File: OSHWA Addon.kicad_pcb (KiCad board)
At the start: 2 copper layers, 33.3 x 40.6 mm, 5 parts, among them J1 Conn_02x02_Counter_Clockwise

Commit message: update silkscreen text
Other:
- board text added: "Andrew Sowa (@junesphd)"
- board text added: "github.com/OSHPark/ ohs18addon"
- board text removed: "Andrew Sowa OSHWA Summit 2018 MIT"
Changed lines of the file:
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@@
-(kicad_pcb (version 20171130) (host pcbnew "(5.0.0)")
+(kicad_pcb (version 20171130) (host pcbnew 5.0.0-fee4fd1~65~ubuntu17.10.1)
   (general
     (thickness 1.6)
-    (drawings 45)
+    (drawings 46)
     (tracks 3)
     (zones 0)
@@
   (page A4)
   (layers
-    (0 F.Cu signal)
-    (31 B.Cu signal)
+    (0 F.Cu signal hide)
+    (31 B.Cu signal hide)
     (32 B.Adhes user)
     (33 F.Adhes user)
@@
       (xy -2.549664 -1.91989) (xy -2.469928 -1.911165) (xy -2.400256 -1.919918)) (layer B.SilkS) (width 0.01))
   )
+  (gr_text "github.com/OSHPark/\nohs18addon" (at 25.49 29.22 90) (layer B.SilkS)
+    (effects (font (size 1 1) (thickness 0.25)) (justify mirror))
+  )
   (gr_text D (at 26 12.73 90) (layer B.SilkS)
     (effects (font (size 1.5 1.5) (thickness 0.3)) (justify mirror))
@@
     (effects (font (size 1 1) (thickness 0.25)) (justify mirror))
   )
-  (gr_text "Andrew Sowa\nOSHWA Summit\n2018 MIT" (at 27 29 90) (layer B.SilkS)
+  (gr_text "Andrew Sowa\n(@junesphd)" (at 11.53 16.78 90) (layer B.SilkS)
     (effects (font (size 1 1) (thickness 0.25)) (justify mirror))
   )

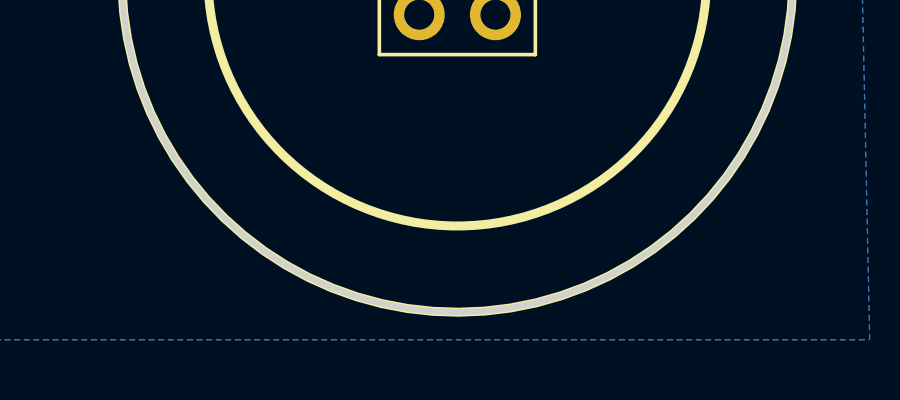
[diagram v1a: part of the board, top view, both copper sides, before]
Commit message: update silkscreen, add line to bottom circle to avoid gerbv bug
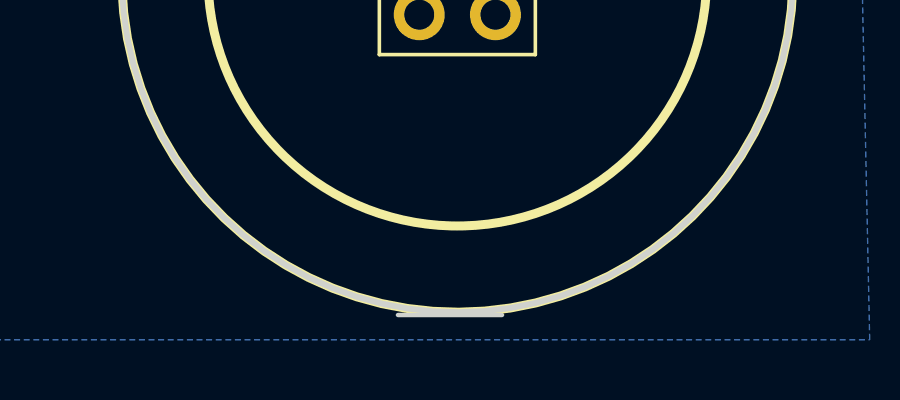
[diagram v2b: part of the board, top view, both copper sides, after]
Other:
- board size 33.3 x 40.6 mm -> 33.3 x 40.7 mm
- board text added: "Design by Andrew Sowa (@junesphd)"
- board text added: "Made by OSH Park"
- board text removed: "Andrew Sowa (@junesphd)"
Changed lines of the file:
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@@
   (general
     (thickness 1.6)
-    (drawings 46)
+    (drawings 48)
     (tracks 3)
     (zones 0)
@@
     (32 B.Adhes user)
     (33 F.Adhes user)
-    (34 B.Paste user)
+    (34 B.Paste user hide)
     (35 F.Paste user)
     (36 B.SilkS user)
@@
       (xy -2.549664 -1.91989) (xy -2.469928 -1.911165) (xy -2.400256 -1.919918)) (layer B.SilkS) (width 0.01))
   )
+  (gr_text "Made by OSH Park" (at 13.97 16.51 90) (layer B.SilkS)
+    (effects (font (size 1 1) (thickness 0.25)) (justify mirror))
+  )
+  (gr_line (start 18.02 40.28) (end 21.49 40.28) (layer Edge.Cuts) (width 0.15))
   (gr_text "github.com/OSHPark/\nohs18addon" (at 25.49 29.22 90) (layer B.SilkS)
     (effects (font (size 1 1) (thickness 0.25)) (justify mirror))
@@
     (effects (font (size 1 1) (thickness 0.25)) (justify mirror))
   )
-  (gr_text "Andrew Sowa\n(@junesphd)" (at 11.53 16.78 90) (layer B.SilkS)
+  (gr_text "Design by Andrew Sowa (@junesphd)" (at 10.922 18.796 90) (layer B.SilkS)
     (effects (font (size 1 1) (thickness 0.25)) (justify mirror))
   )

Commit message: update silkscreen
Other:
- board text added: "Made by OSH Park for OHS 2018"
- board text removed: "Made by OSH Park"
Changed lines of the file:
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@@
   (page A4)
   (layers
-    (0 F.Cu signal hide)
+    (0 F.Cu signal)
     (31 B.Cu signal hide)
     (32 B.Adhes user)
@@
       (xy -2.549664 -1.91989) (xy -2.469928 -1.911165) (xy -2.400256 -1.919918)) (layer B.SilkS) (width 0.01))
   )
-  (gr_text "Made by OSH Park" (at 13.97 16.51 90) (layer B.SilkS)
+  (gr_text "Made by OSH Park for OHS 2018" (at 13.716 22.86 90) (layer B.SilkS)
     (effects (font (size 1 1) (thickness 0.25)) (justify mirror))
   )
